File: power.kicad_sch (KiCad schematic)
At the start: 43 parts, among them J14 Molex_Nano-Fit_1x2_105309-1202, Q2 PJE138K, Q3 PJE138K, Q4 SI2337DS, U3 AP62301_TSOT

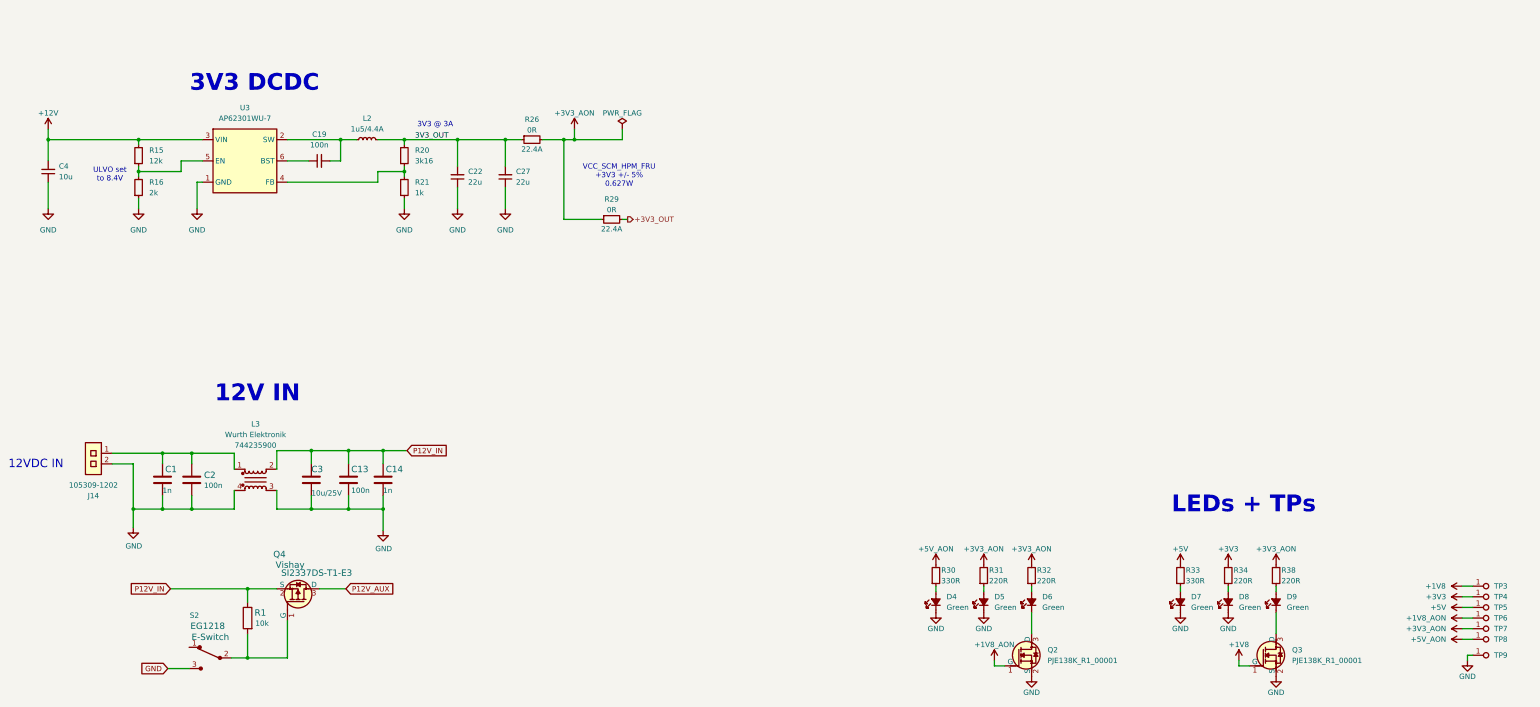
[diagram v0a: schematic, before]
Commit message: [#92504] Remove micro USB and USB A
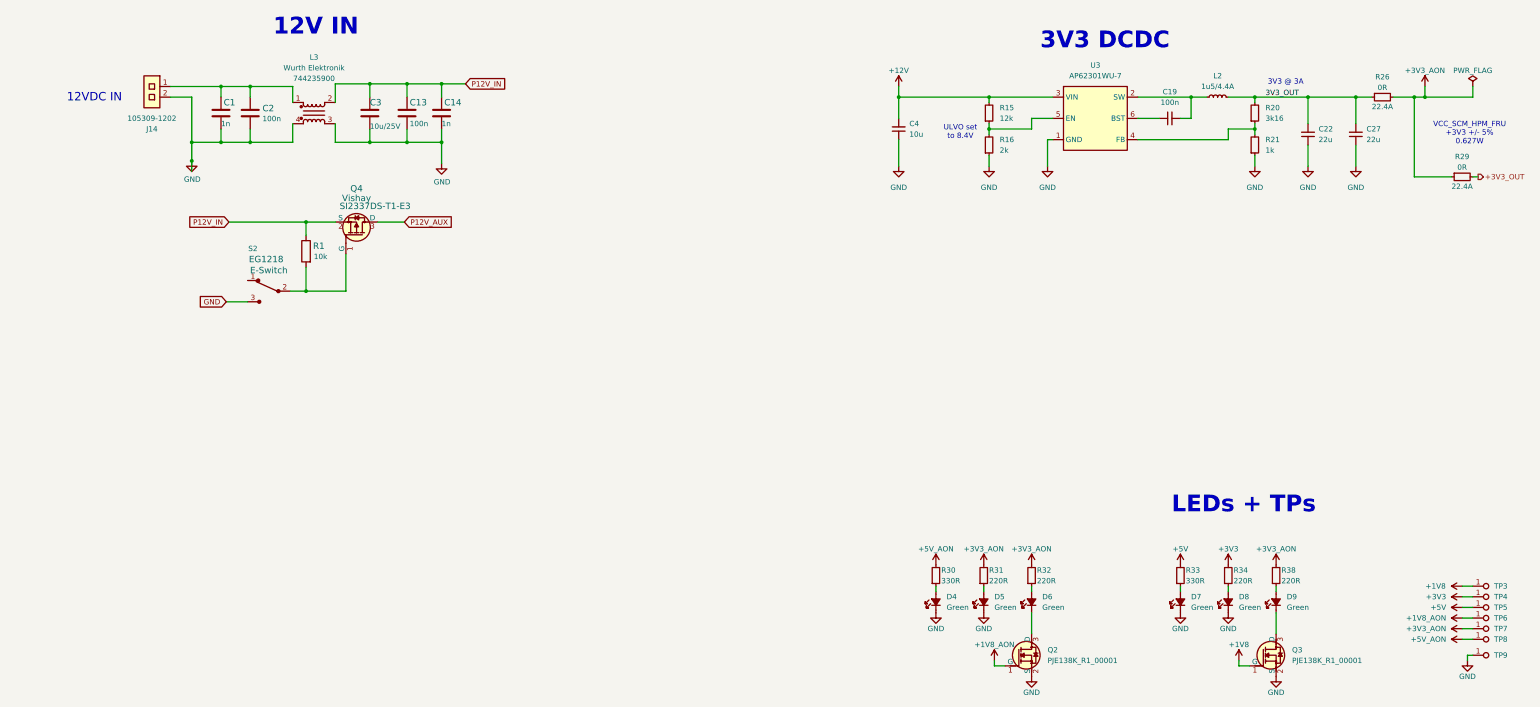
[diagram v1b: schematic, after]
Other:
- moved on the sheet: C1, C13, C14, C19, C2, C22, C27, C3, C4, J14, L2, L3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

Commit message: [#92504] Add 12V power to DCM-SCM
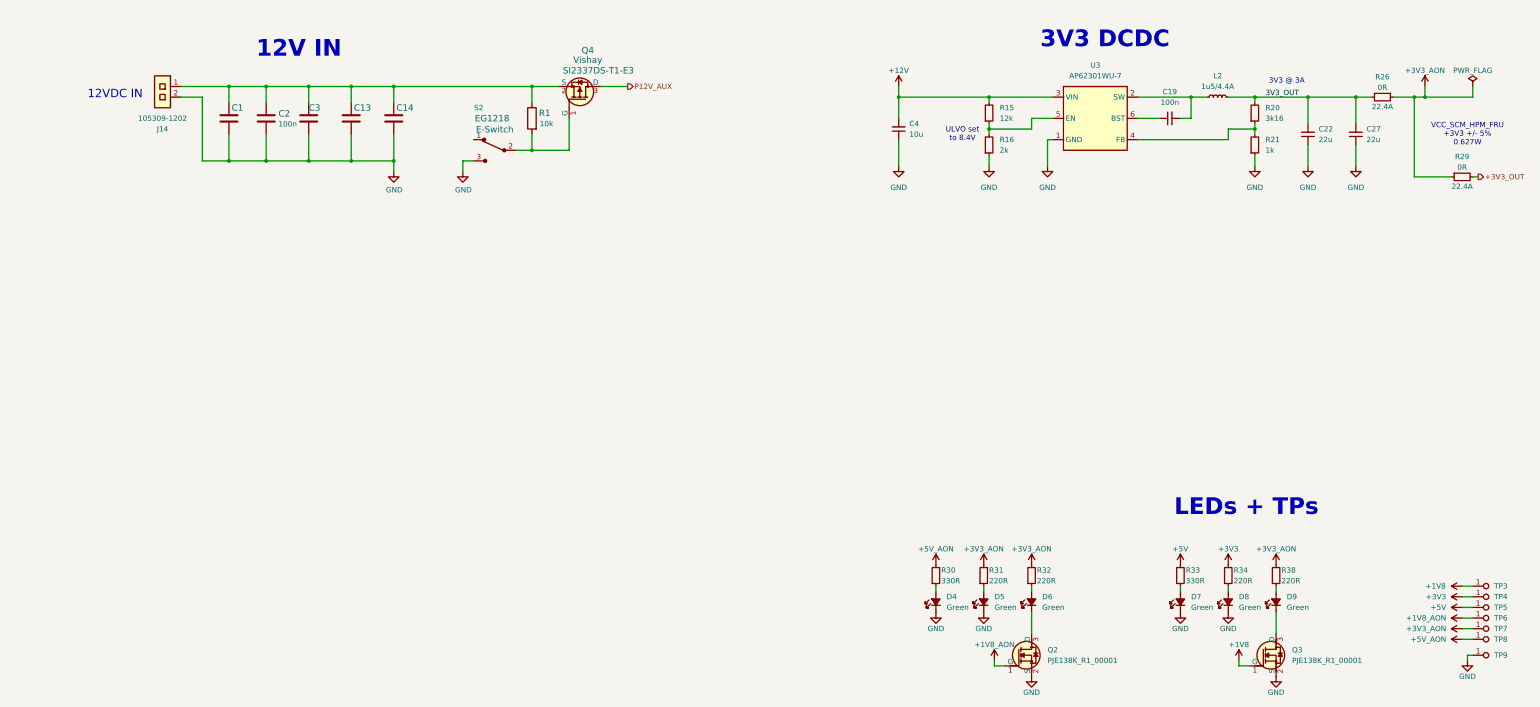
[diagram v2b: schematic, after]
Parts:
- removed L3: 744235900, bmc-breakout-board-footprints:744235900, symbol bmc-breakout-board:744235900
- J14: footprint antmicro-footprints:PinHeader_2x7_P2mm_Drill0.9mm_878311420 -> antmicro-footprints:Conn_Molex_Nano-Fit_1x2_105313-2202_Compliant_105309-2202
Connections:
- net P12V_IN is gone; now on an unnamed net: C13.1, C14.1, C3.1, Q4.2 (S), R1.1
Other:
- moved on the sheet: C1, C13, C14, C2, C3, J14, Q4, R1, S2

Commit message: [#92504] Add 3V3 DCDC converter
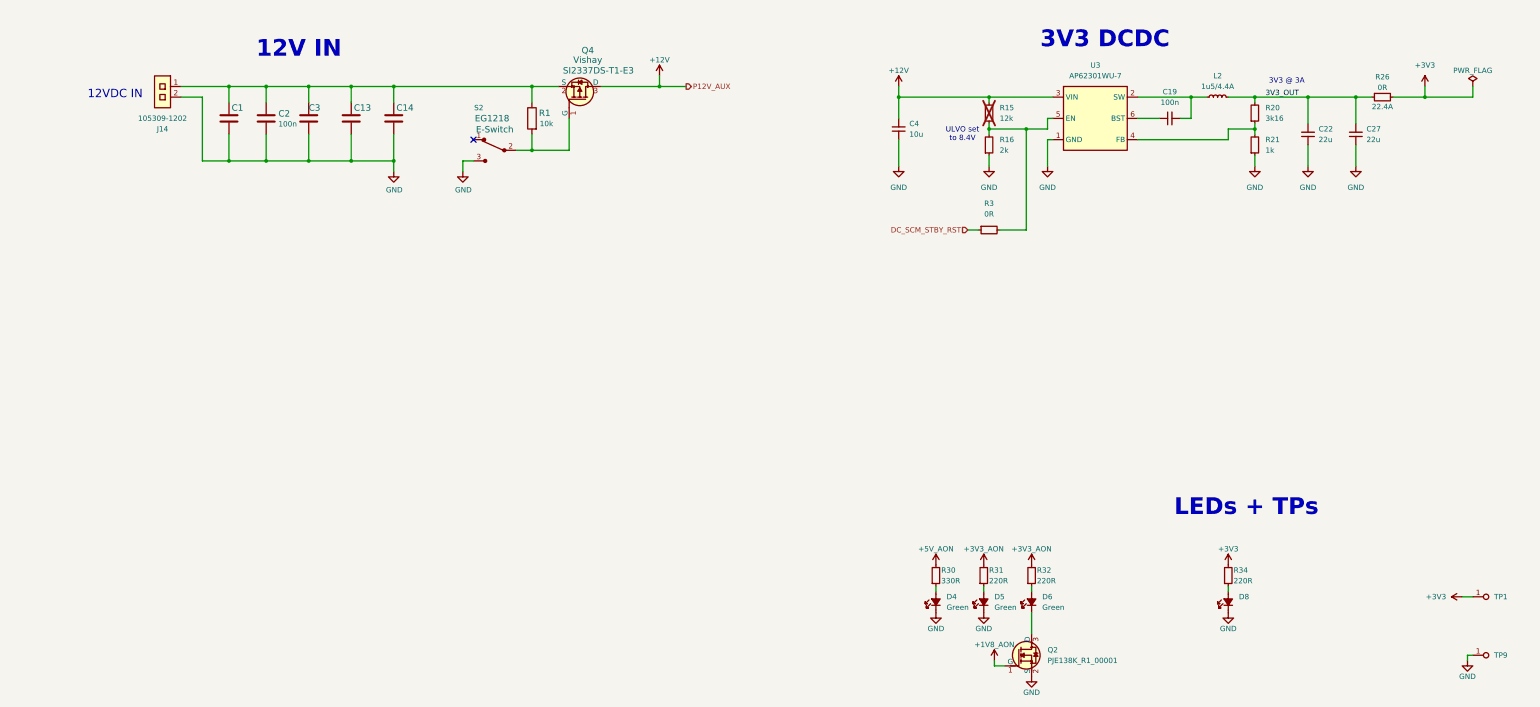
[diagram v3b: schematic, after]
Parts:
- removed D7, D9: LED_G_0402_VLMTG1500-GS08, antmicro-footprints:LED_0402_1005Metric_G, symbol antmicroLEDIndicationDiscrete:LED_G_0402_VLMTG1500-GS08
- removed Q3: PJE138K, antmicro-footprints:SOT-523, symbol antmicroTransistorsFETsMOSFETsSingle:PJE138K
- removed R29: R_0R_22.4A_0603, antmicro-footprints:R_0603_1608Metric, symbol antmicroResistors0603:R_0R_22.4A_0603
- removed R33: R_330R_0402, antmicro-footprints:R_0402_1005Metric, symbol antmicroResistors0402:R_330R_0402
- removed R38: R_220R_0402, antmicro-footprints:R_0402_1005Metric, symbol antmicroResistors0402:R_220R_0402
- removed TP3, TP5, TP6, TP7, TP8: TP_0.75mm_SMD, antmicro-footprints:TP_SMD_0.75mm, symbol antmicroTestPoints:TP_0.75mm_SMD
- added R3: R_0R_0402, antmicro-footprints:R_0402_1005Metric, symbol antmicroResistors0402:R_0R_0402
- R15: now not fitted
- renumbered TP4 to TP1
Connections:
- net P12V_AUX is gone; now on net +12V: Q4.3 (D)
- net +3V3: now also R26.2
- net +3V3_AON: no longer R26.2
- net at R15.1, R16.2, U3.5 (EN): now also R3.2
- new net DC_SCM_STBY_RST: R3.1
- no-connect marks 0 -> 1
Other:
- note removed: "VCC_SCM_HPM_FRU +3V3 +/- 5% 0.627W"

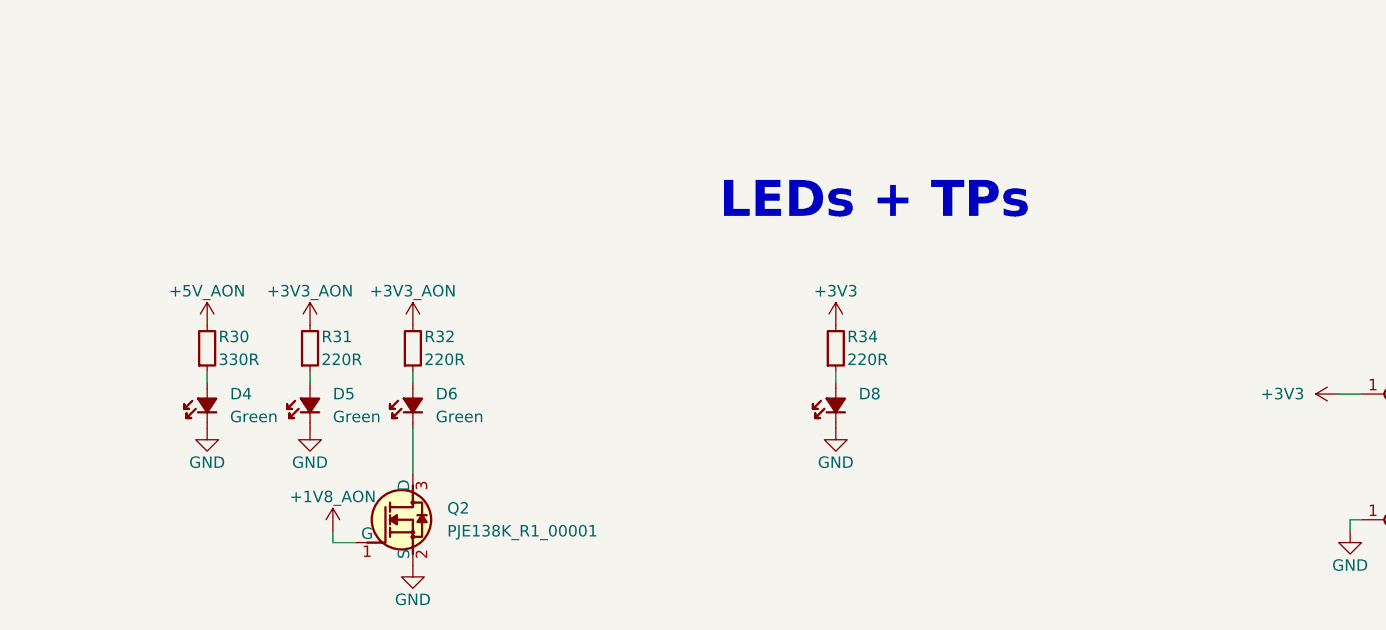
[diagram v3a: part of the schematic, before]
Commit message: [#92504] Add temperature sensor
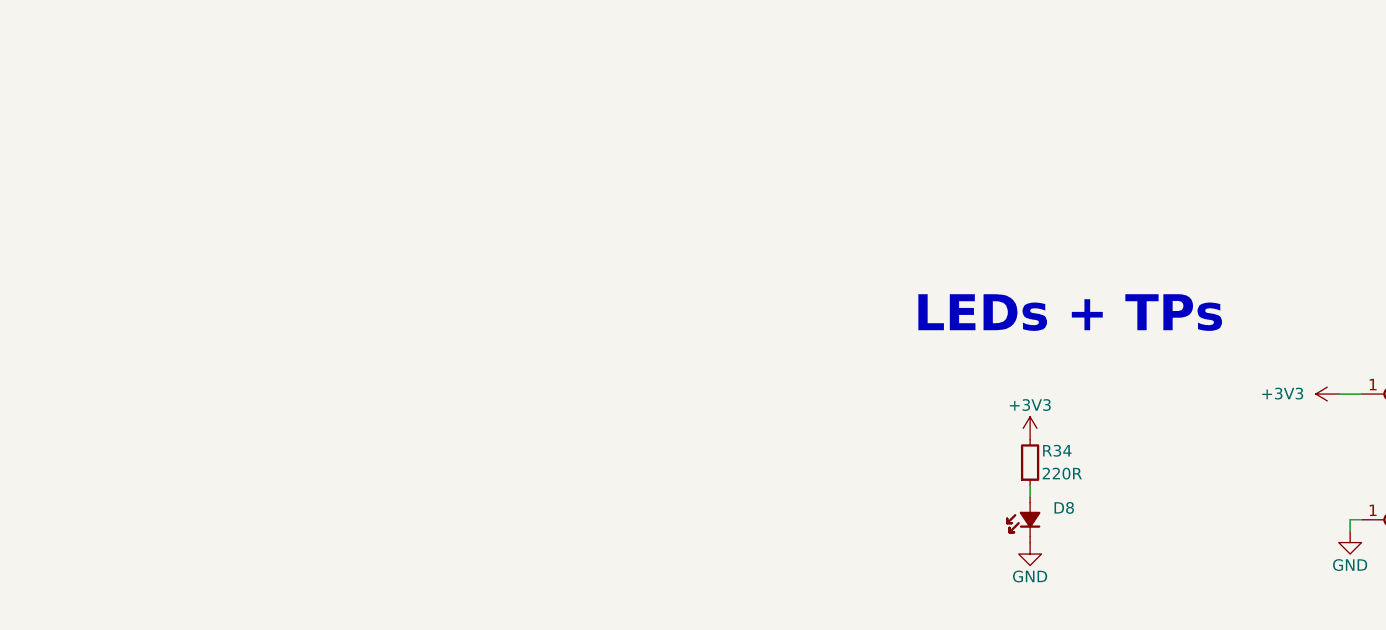
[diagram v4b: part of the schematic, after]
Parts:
- removed D4, D5, D6: LED_G_0402_VLMTG1500-GS08, antmicro-footprints:LED_0402_1005Metric_G, symbol antmicroLEDIndicationDiscrete:LED_G_0402_VLMTG1500-GS08
- removed Q2: PJE138K, antmicro-footprints:SOT-523, symbol antmicroTransistorsFETsMOSFETsSingle:PJE138K
- removed R30: R_330R_0402, antmicro-footprints:R_0402_1005Metric, symbol antmicroResistors0402:R_330R_0402
- removed R31, R32: R_220R_0402, antmicro-footprints:R_0402_1005Metric, symbol antmicroResistors0402:R_220R_0402
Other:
- moved on the sheet: D8, R34

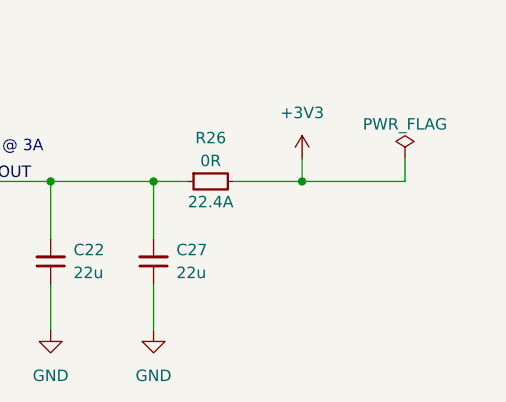
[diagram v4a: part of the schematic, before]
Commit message: [#92504] Add LTPI connector
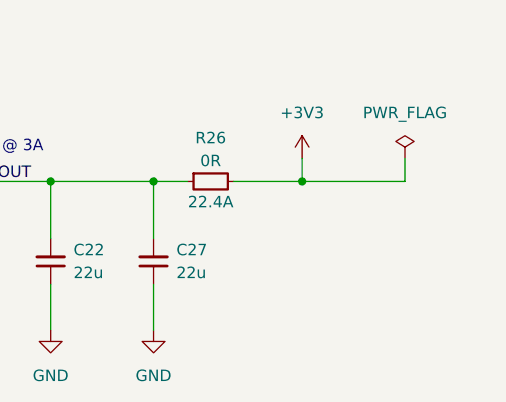
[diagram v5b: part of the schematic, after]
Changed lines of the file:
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@@
 	)
 	(symbol
-		(lib_id "antmicropower:PWR_FLAG")
-		(at 381 73.66 0)
-		(unit 1)
-		(exclude_from_sim no)
-		(in_bom yes)
-		(on_board yes)
-		(dnp no)
-		(property "Reference" "#FLG04"
-			(at 381 71.755 0)
-			(effects
-				(font
-					(size 1.27 1.27)
-				)
-				(hide yes)
-			)
-		)
-		(property "Value" "PWR_FLAG"
-			(at 381 69.85 0)
-			(effects
-				(font
-					(size 1.27 1.27)
-				)
-			)
-		)
-		(property "Footprint" ""
-			(at 381 73.66 0)
-			(effects
-				(font
-					(size 1.27 1.27)
-				)
-				(hide yes)
-			)
-		)
-		(property "Datasheet" ""
-			(at 381 73.66 0)
-			(effects
-				(font
-					(size 1.27 1.27)
-				)
-				(hide yes)
-			)
-		)
-		(property "Description" ""
-			(at 381 73.66 0)
-			(effects
-				(font
-					(size 1.27 1.27)
-				)
-				(hide yes)
-			)
-		)
-		(pin "1"
-		)
-		(instances
-			(project "bmc-breakout-board"
-				(path "/5d67ef28-5805-4f87-b722-2926dabf7f6e/6a40469a-13ae-4d69-8a2b-3c10ffcd9800"
-					(reference "#FLG04")
-					(unit 1)
-				)
-			)
-		)
-	)
-	(symbol
 		(lib_id "antmicroDCDCConverters:AP62301_TSOT")
 		(at 280.67 76.2 0)
@@
 					(unit 1)
 				)
+			)
+		)
+	)
+	(symbol
+		(lib_name "PWR_FLAG_1")
+		(lib_id "antmicropower:PWR_FLAG")
+		(at 381 73.66 0)
+		(unit 1)
+		(exclude_from_sim no)
+		(in_bom yes)
+		(on_board yes)
+		(dnp no)
+		(fields_autoplaced yes)
+		(property "Reference" "#FLG03"
+			(at 381 71.755 0)
+			(effects
+				(font
+					(size 1.27 1.27)
+				)
+				(hide yes)
+			)
+		)
+		(property "Value" "PWR_FLAG"
+			(at 381 68.58 0)
+			(effects
+				(font
+					(size 1.27 1.27)
+				)
+			)
+		)
+		(property "Footprint" ""
+			(at 381 73.66 0)
+			(effects
+				(font
+					(size 1.27 1.27)
+				)
+				(hide yes)
+			)
+		)
+		(property "Datasheet" ""
+			(at 381 73.66 0)
+			(effects
+				(font
+					(size 1.27 1.27)
+				)
+				(hide yes)
+			)
+		)
+		(property "Description" ""
+			(at 381 76.2 0)
+			(effects
+				(font
+					(size 1.27 1.27)
+				)
+				(justify left bottom)
+				(hide yes)
+			)
+		)
+		(pin "1"
+		)
+		(instances
+			(project ""
+				(path "/5d67ef28-5805-4f87-b722-2926dabf7f6e/6a40469a-13ae-4d69-8a2b-3c10ffcd9800"
+					(reference "#FLG03")
+					(unit 1)
+				)

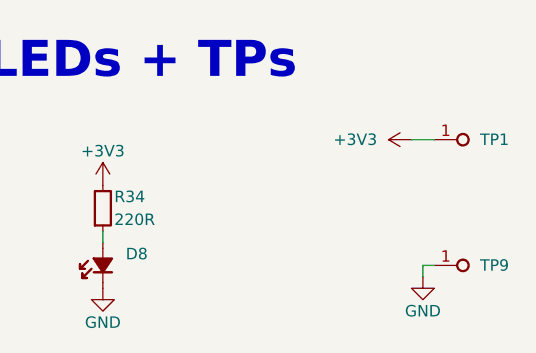
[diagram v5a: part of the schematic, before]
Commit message: [#92504] Connect QWIIC connector
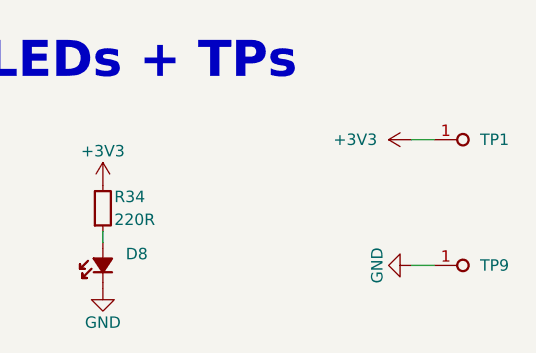
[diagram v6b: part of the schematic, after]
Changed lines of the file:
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@@
 	(wire
 		(pts
-			(xy 381 209.55) (xy 379.73 209.55)
+			(xy 381 209.55) (xy 378.46 209.55)
 		)
 		(stroke
@@
 		(pts
 			(xy 102.87 85.09) (xy 102.87 91.44)
-		)
-		(stroke
-			(width 0)
-			(type default)
-		)
-	)
-	(wire
-		(pts
-			(xy 379.73 209.55) (xy 379.73 210.82)
 		)
 		(stroke
@@
 	(symbol
 		(lib_id "antmicropower:GND")
-		(at 379.73 210.82 0)
+		(at 378.46 209.55 270)
 		(unit 1)
 		(exclude_from_sim no)
@@
 		(dnp no)
 		(property "Reference" "#PWR081"
-			(at 388.62 213.36 0)
+			(at 375.92 218.44 0)
 			(effects
 				(font
@@
 		)
 		(property "Value" "GND"
-			(at 379.73 214.63 0)
+			(at 374.65 209.55 0)
 			(effects
 				(font
@@
 		)
 		(property "Footprint" ""
-			(at 388.62 218.44 0)
+			(at 370.84 218.44 0)
 			(effects
 				(font
@@
 		)
 		(property "Datasheet" ""
-			(at 388.62 223.52 0)
+			(at 365.76 218.44 0)
 			(effects
 				(font
@@
 		)
 		(property "Description" ""
-			(at 379.73 210.82 0)
+			(at 378.46 209.55 0)
 			(effects
 				(font
@@
 		)
 		(property "Author" "Antmicro"
-			(at 388.62 218.44 0)
+			(at 370.84 218.44 0)
 			(effects
 				(font
@@
 		)
 		(property "License" "Apache-2.0"
-			(at 388.62 220.98 0)
-			(effects
-				(font
+			(at 368.3 218.44 0)
+			(effects
+				(font
